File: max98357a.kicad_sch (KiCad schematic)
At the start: 17 parts, among them U5 MAX98357A

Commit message: add files update
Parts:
- L4, L5, L6: value ferrite -> 100mH
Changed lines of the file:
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@@
 			)
 		)
-		(property "Value" "ferrite"
+		(property "Value" "100mH"
 			(at 181.61 83.8199 0)
 			(show_name no)
@@
 			)
 		)
-		(property "Value" "ferrite"
+		(property "Value" "100mH"
 			(at 213.36 104.14 90)
 			(show_name no)
@@
 			)
 		)
-		(property "Description" "Inductor"
+		(property "Description" "Inductor 100mH"
 			(at 213.36 106.68 0)
 			(hide yes)
@@
 			)
 		)
-		(property "Value" "ferrite"
+		(property "Value" "100mH"
 			(at 227.33 107.95 90)
 			(show_name no)
@@
 			)
 		)
-		(property "Description" "Inductor"
+		(property "Description" "Inductor 100mH"
 			(at 227.33 110.49 0)
 			(hide yes)

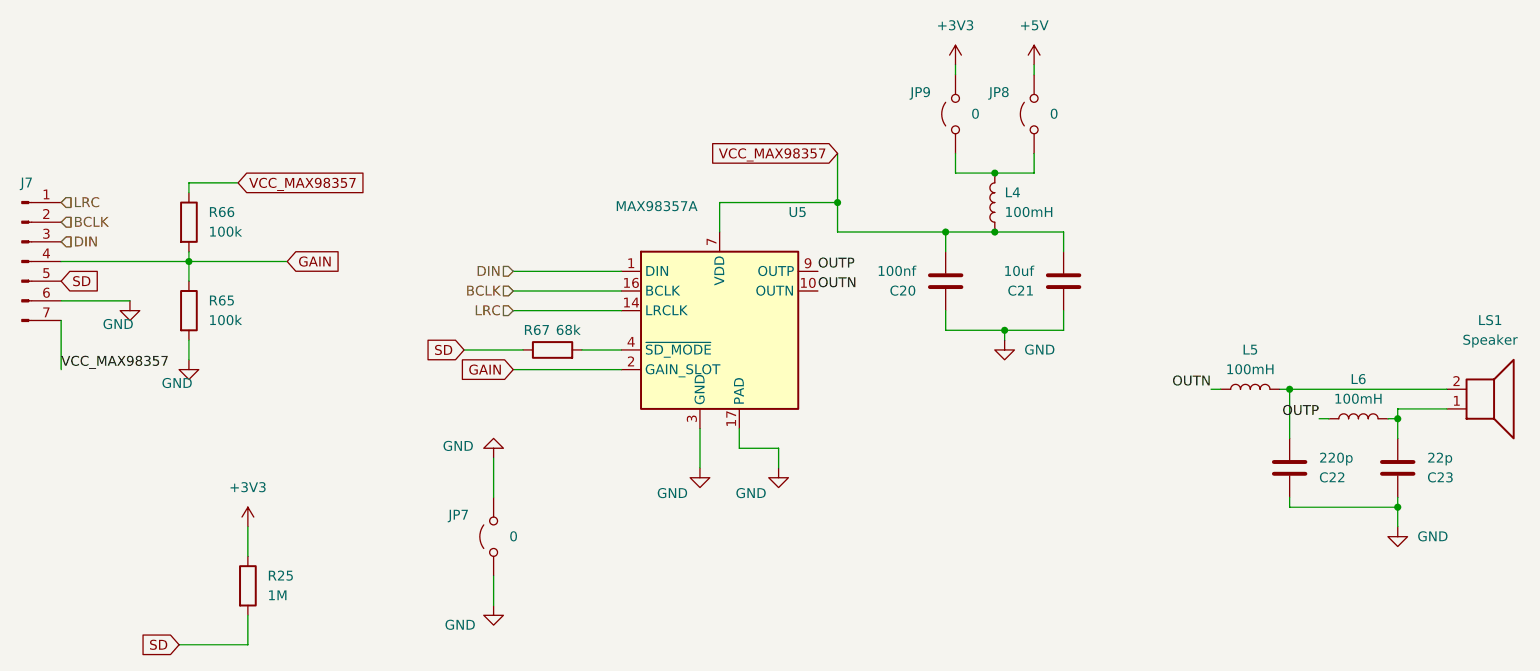
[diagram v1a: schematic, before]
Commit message: Actualización de esquemas y PCB con datos LCSC y librerías JLC
- Añade propiedades LCSC a los símbolos de las hojas de esquema
- Actualiza las hojas TXS0108E, display, esp32_c6, ft232, inmp441,
  led_sw_gpio, max98357a, micro_sd, power_supply y el esquema raíz
- Reorganiza el PCB (footprints, jumpers y nets) y actualiza el proyecto
- Incluye las librerías locales JLCImport (símbolos, huellas y modelos 3D)
  y las entradas correspondientes en fp-lib-table y sym-lib-table
- Añade la documentación técnica en docs/ y el archivo de posiciones
  esp32_xiaozhi-all.pos
- Elimina los ZIP generados gebers.zip y production.zip
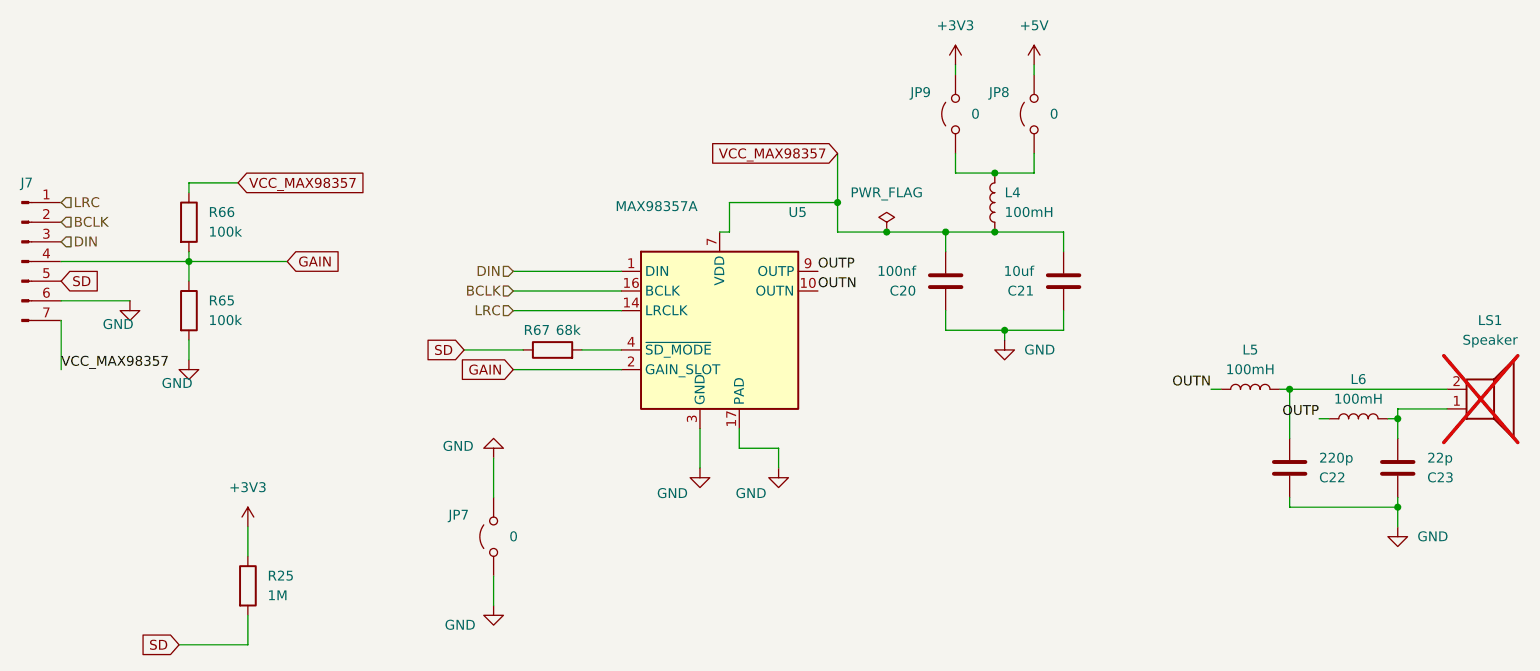
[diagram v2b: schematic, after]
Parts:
- C20: LCSC (none) -> C1525
- C21: LCSC (none) -> C15850
- C22: LCSC (none) -> C107145
- C23: LCSC (none) -> C1804
- J7, JP7, JP8, JP9: now left out of the parts list
- L4, L5, L6: LCSC (none) -> C1015
- LS1: now not fitted; now left out of the parts list
- R25: LCSC (none) -> C17514
- R65, R66: LCSC (none) -> C149504
- R67: LCSC (none) -> C17801
- U5: LCSC (none) -> C910544

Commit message: Actualización de esquemas, PCB y librerías
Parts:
- C20: LCSC C1525 -> C28233
- C22: LCSC C107145 -> C107145
- C23: value 22p -> 220p; LCSC C1804 -> C107145
- JP8: footprint Jumper:SolderJumper-2_P1.3mm_Open_RoundedPad1.0x1.5mm -> Jumper:SolderJumper-2_P1.3mm_Bridged_RoundedPad1.0x1.5mm
- L4: footprint Inductor_SMD:L_0805_2012Metric -> Inductor_SMD:L_1210_3225Metric; LCSC C1015 -> C1882517
- L5, L6: value 100mH -> 100uH; LCSC C1015 -> C845118
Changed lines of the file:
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@@
 	(wire
 		(pts
-			(xy 146.05 82.55) (xy 160.02 82.55)
+			(xy 144.78 82.55) (xy 160.02 82.55)
 		)
 		(stroke
@@
 	(wire
 		(pts
-			(xy 146.05 86.36) (xy 144.78 86.36)
+			(xy 189.23 88.9) (xy 189.23 86.36)
 		)
 		(stroke
@@
 	(wire
 		(pts
-			(xy 189.23 88.9) (xy 189.23 86.36)
+			(xy 173.99 88.9) (xy 173.99 86.36)
 		)
 		(stroke
@@
 	(wire
 		(pts
-			(xy 173.99 88.9) (xy 173.99 86.36)
-		)
-		(stroke
-			(width 0)
-			(type default)
-		)
-	)
-	(wire
-		(pts
-			(xy 146.05 82.55) (xy 146.05 86.36)
+			(xy 144.78 82.55) (xy 144.78 86.36)
 		)
 		(stroke
@@
 			)
 		)
-		(property "Footprint" "Inductor_SMD:L_0805_2012Metric"
+		(property "Footprint" "Inductor_SMD:L_1210_3225Metric"
 			(at 180.34 82.55 0)
 			(hide yes)
@@
 			)
 		)
-		(property "LCSC" "C1015"
+		(property "LCSC" "C1882517"
 			(at 180.34 82.55 0)
 			(hide yes)
@@
 			)
 		)
-		(property "Value" "22p"
+		(property "Value" "220p"
 			(at 236.22 115.57 0)
 			(show_name no)
@@
 			)
 		)
-		(property "LCSC" "C1804"
+		(property "LCSC" "C107145"
 			(at 232.41 116.84 0)
 			(hide yes)
@@
 			)
 		)
-		(property "LCSC" "C1525"
+		(property "LCSC" "C28233"
 			(at 173.99 92.71 0)
 			(hide yes)
@@
 			)
 		)
-		(property "LCSC" "C107145 "
+		(property "LCSC" "C107145"
 			(at 218.44 116.84 0)
 			(hide yes)
@@
 			)
 		)
-		(property "Footprint" "Jumper:SolderJumper-2_P1.3mm_Open_RoundedPad1.0x1.5mm"
+		(property "Footprint" "Jumper:SolderJumper-2_P1.3mm_Bridged_RoundedPad1.0x1.5mm"
 			(at 185.42 71.12 0)
 			(hide yes)
@@
 			)
 		)
-		(property "Value" "100mH"
+		(property "Value" "100uH"
 			(at 213.36 104.14 90)
 			(show_name no)
@@
 			)
 		)
-		(property "LCSC" "C1015"
+		(property "LCSC" "C845118"
 			(at 213.36 106.68 90)
 			(hide yes)
@@
 			)
 		)
-		(property "Value" "100mH"
+		(property "Value" "100uH"
 			(at 227.33 107.95 90)
 			(show_name no)
@@
 			)
 		)
-		(property "LCSC" "C1015"
+		(property "LCSC" "C845118"
 			(at 227.33 110.49 90)
 			(hide yes)

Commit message: correccion de numero de partes de componentes
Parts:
- L4: value 100mH -> 10uH @ 305mΩ; footprint Inductor_SMD:L_1210_3225Metric -> Inductor_SMD:L_1210_3225Metri
- L5, L6: value 100uH -> 100mΩ 2A 600Ω@100MHz
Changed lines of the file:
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@@
 			)
 		)
-		(property "Value" "100mH"
+		(property "Value" "10uH  @ 305mΩ"
 			(at 181.61 83.8199 0)
 			(show_name no)
@@
 			)
 		)
-		(property "Footprint" "Inductor_SMD:L_1210_3225Metric"
+		(property "Footprint" "Inductor_SMD:L_1210_3225Metri"
 			(at 180.34 82.55 0)
 			(hide yes)
@@
 			)
 		)
-		(property "Description" "Inductor"
+		(property "Description" "1.4A 1.6A 10uH 305mΩ ±20% 1210 Inductors"
 			(at 180.34 82.55 0)
 			(hide yes)
@@
 		(in_bom no)
 		(on_board yes)
-		(in_pos_files yes)
+		(in_pos_files no)
 		(dnp no)
 		(property "Reference" "JP9"
@@
 		(in_bom no)
 		(on_board yes)
-		(in_pos_files yes)
+		(in_pos_files no)
 		(dnp no)
 		(property "Reference" "JP7"
@@
 		(in_bom no)
 		(on_board yes)
-		(in_pos_files yes)
+		(in_pos_files no)
 		(dnp no)
 		(fields_autoplaced yes)
@@
 		(in_bom no)
 		(on_board yes)
-		(in_pos_files yes)
+		(in_pos_files no)
 		(dnp no)
 		(property "Reference" "JP8"
@@
 			)
 		)
-		(property "Value" "100uH"
+		(property "Value" "100mΩ 2A 600Ω@100MHz"
 			(at 213.36 104.14 90)
 			(show_name no)
@@
 			)
 		)
-		(property "Description" "Inductor 100mH"
+		(property "Description" "100mΩ 2A 600Ω@100MHz"
 			(at 213.36 106.68 0)
 			(hide yes)
@@
 			)
 		)
-		(property "Value" "100uH"
+		(property "Value" "100mΩ 2A 600Ω@100MHz"
 			(at 227.33 107.95 90)
 			(show_name no)
@@
 			)
 		)
-		(property "Description" "Inductor 100mH"
+		(property "Description" "-55℃~+125℃ 1 100mΩ 2A 600Ω@100MHz ±25% 0805 Ferrite Beads ROHS"
 			(at 227.33 110.49 0)
 			(hide yes)

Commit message: add update
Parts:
- L4: value 10uH @ 305mΩ -> TFM322512ALVA100MTAA
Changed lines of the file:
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@@
 			)
 		)
-		(property "Value" "10uH  @ 305mΩ"
+		(property "Value" "TFM322512ALVA100MTAA"
 			(at 181.61 83.8199 0)
 			(show_name no)

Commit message: update sch & pcb
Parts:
- L4: footprint Inductor_SMD:L_1210_3225Metri -> Inductor_SMD:L_1210_3225Metric
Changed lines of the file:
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@@
 			)
 		)
-		(property "Footprint" "Inductor_SMD:L_1210_3225Metri"
+		(property "Footprint" "Inductor_SMD:L_1210_3225Metric"
 			(at 180.34 82.55 0)
 			(hide yes)
